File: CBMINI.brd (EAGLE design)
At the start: 100 x 60 mm, 47 parts, among them J1 USB_B_PTH, SW1 SWITCH-DPDT3, U1 MCP2551, X1 INPUT, X2 OUTPUT

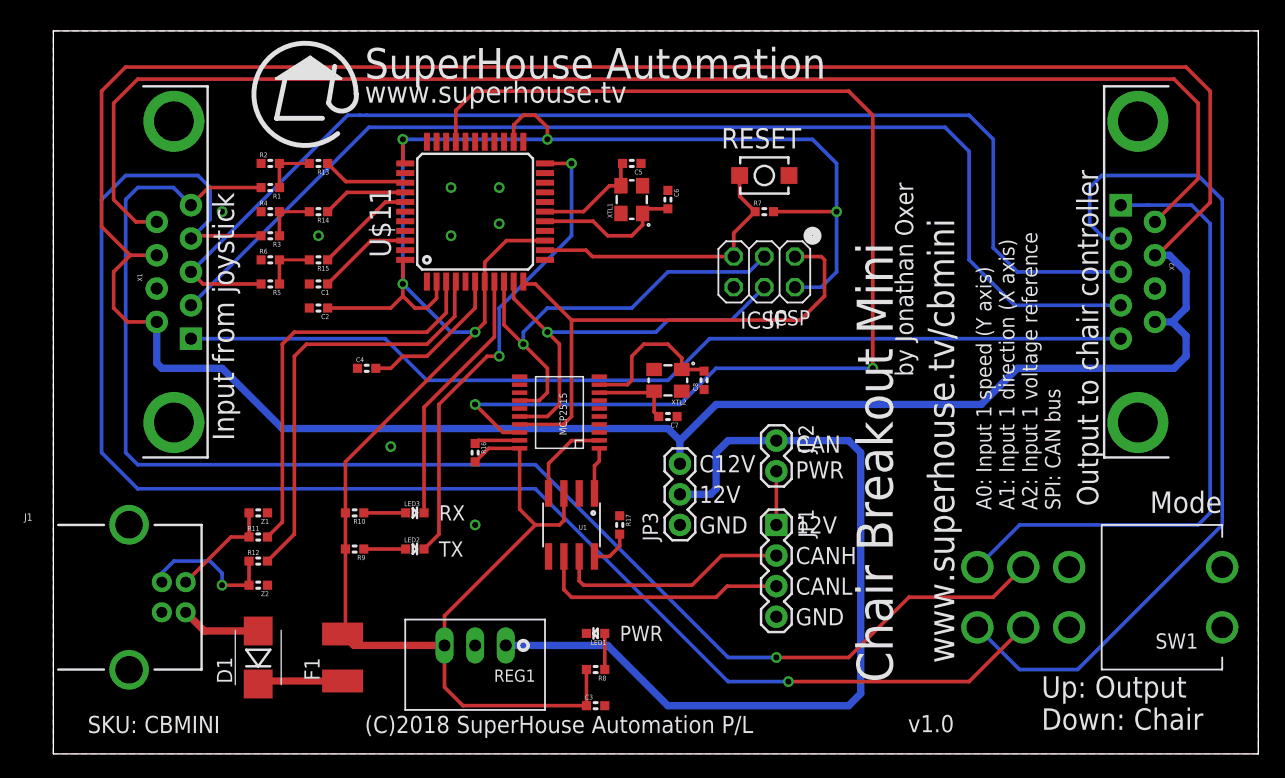
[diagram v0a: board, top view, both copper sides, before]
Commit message: Added CAN bus interrupt connection to D2 for v1.1 release
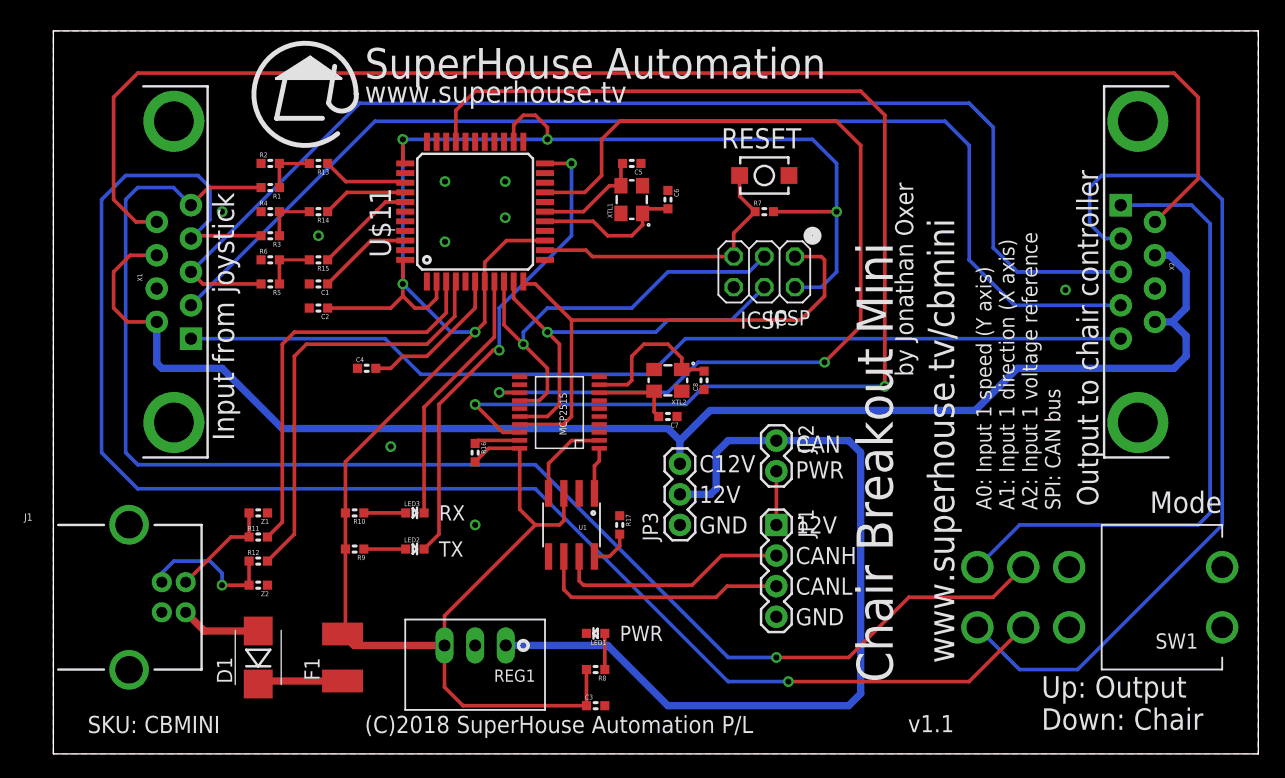
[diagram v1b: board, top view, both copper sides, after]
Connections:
- removed net INT: U$4.13
- net D2_SDA: now also U$4.13
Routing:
- net C12V: track 244.0 -> 120.3 mm
- net D2_SDA: track 0.00 -> 80.2 mm, vias 0 -> 2
- net D10_A11: track 98.6 -> 101.5 mm
- net REFERENCE: track 99.4 -> 100.8 mm
- net N$1: track 115.3 -> 116.3 mm
- net N$6: track 94.7 -> 95.4 mm
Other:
- board text added: "v1.1"
- board text removed: "v1.0"
